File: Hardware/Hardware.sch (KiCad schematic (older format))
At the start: 68 parts

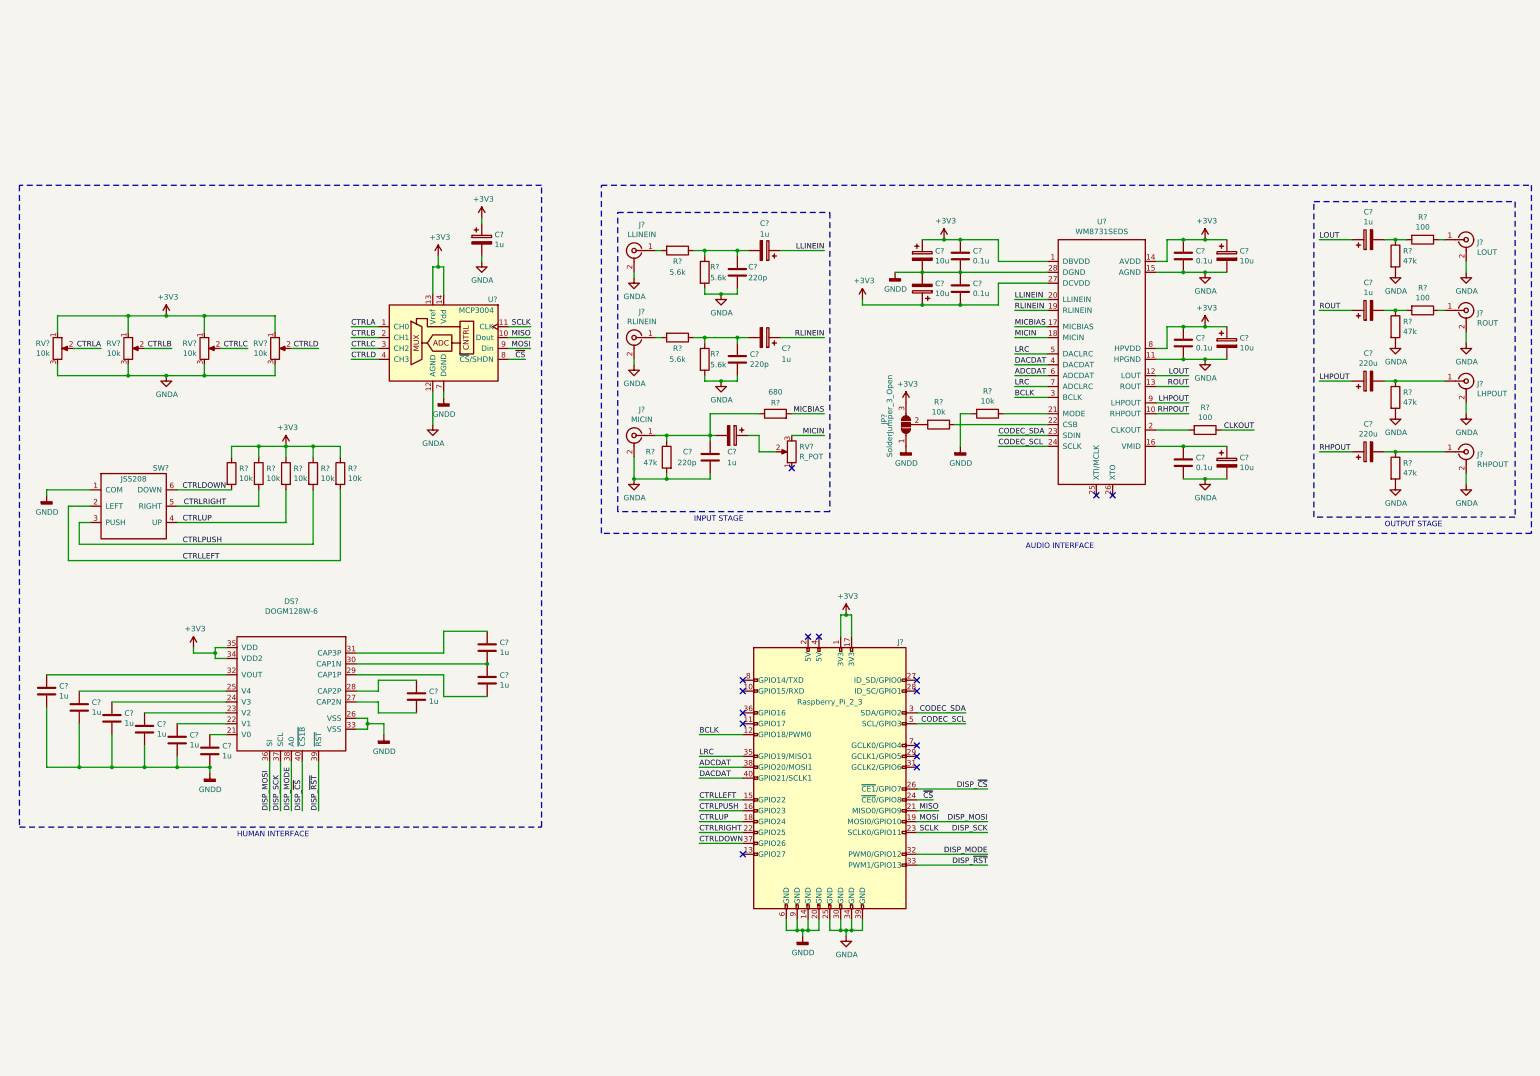
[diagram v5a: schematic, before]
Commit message: Assigned PCB footprints to schematic symbols
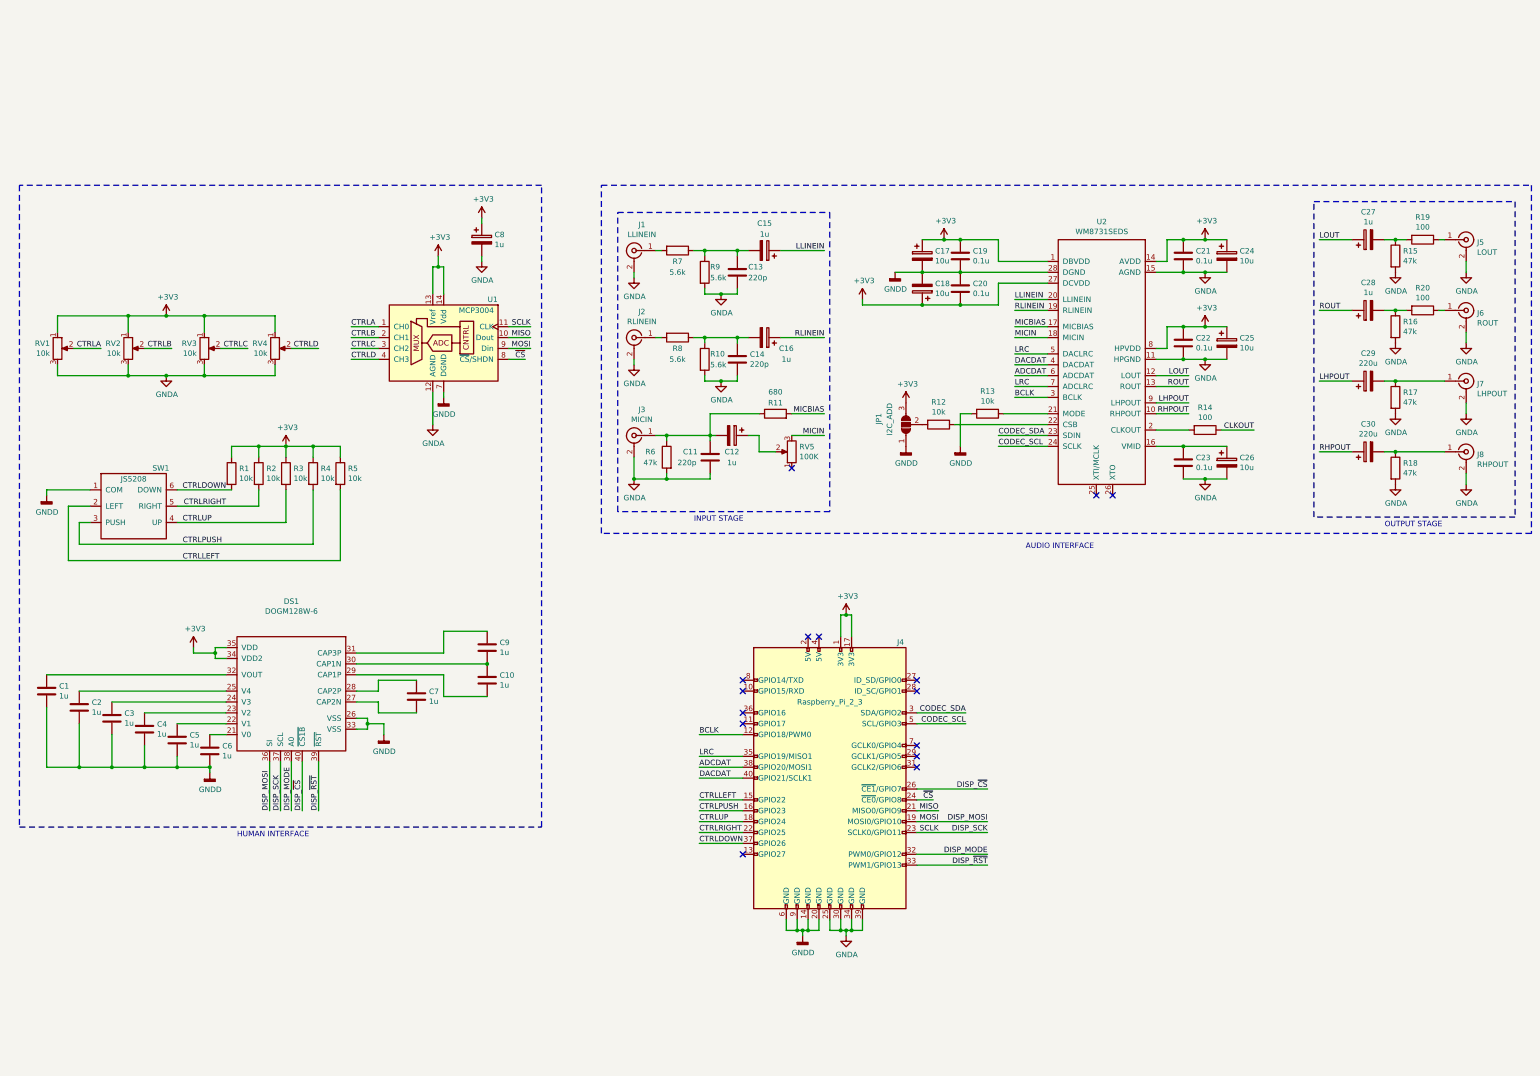
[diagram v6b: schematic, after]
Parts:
- C1, C10, C11, C13, C14, C2, C3, C4, C5, C6, C7, C9: renamed from C?; footprint (none) -> Capacitor_SMD:C_0603_1608Metric_Pad1.05x0.95mm_HandSolder
- C12, C15, C16, C27, C28, C8: renamed from C?; footprint (none) -> Capacitor_Tantalum_SMD:CP_EIA-3528-12_Kemet-T_Pad1.50x2.35mm_HandSolder
- C17, C18, C24, C25, C26: renamed from C?; footprint (none) -> Capacitor_Tantalum_SMD:CP_EIA-7343-15_Kemet-W_Pad2.25x2.55mm_HandSolder
- C19, C20, C21, C22, C23: renamed from C?; footprint (none) -> Capacitor_SMD:C_0805_2012Metric_Pad1.15x1.40mm_HandSolder
- C29, C30: renamed from C?; footprint (none) -> Capacitor_SMD:CP_Elec_8x10
- DS1: renamed from DS?; footprint (none) -> signl:DOGM128W
- J1, J2, J3, J5, J6, J7, J8: renamed from J?; footprint (none) -> Connector_Molex:Molex_KK-254_AE-6410-02A_1x02_P2.54mm_Vertical
- JP1: renamed from JP?; value SolderJumper_3_Open -> I2C_ADD; footprint (none) -> Jumper:SolderJumper-3_P1.3mm_Open_RoundedPad1.0x1.5mm_NumberLabels
- R1, R10, R11, R12, R13, R14, R15, R16, R17, R18, R19, R2, R20, R3, R4, R5, R6, R7, R8, R9: renamed from R?; footprint (none) -> Resistor_SMD:R_0805_2012Metric_Pad1.15x1.40mm_HandSolder
- RV1, RV2, RV3, RV4: renamed from RV?; footprint (none) -> Connector_Molex:Molex_KK-254_AE-6410-03A_1x03_P2.54mm_Vertical
- RV5: renamed from RV?; value R_POT -> 100K; footprint (none) -> Connector_Molex:Molex_KK-254_AE-6410-03A_1x03_P2.54mm_Vertical
- SW1: renamed from SW?; footprint (none) -> signl:JS5208
- gave numbers to parts that had none: 3

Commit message: Changed to using 3-pin connectors for LINEIN and HP. Footprint associations, Schematic PDF, Netlist updated.
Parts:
- removed J1: LLINEIN, Connector_Molex:Molex_KK-254_AE-6410-02A_1x02_P2.54mm_Vertical, symbol Connector:Conn_Coaxial
- removed J2: RLINEIN, Connector_Molex:Molex_KK-254_AE-6410-02A_1x02_P2.54mm_Vertical, symbol Connector:Conn_Coaxial
- removed J5: LOUT, Connector_Molex:Molex_KK-254_AE-6410-02A_1x02_P2.54mm_Vertical, symbol Connector:Conn_Coaxial
- removed J6: ROUT, Connector_Molex:Molex_KK-254_AE-6410-02A_1x02_P2.54mm_Vertical, symbol Connector:Conn_Coaxial
- removed J7: LHPOUT, Connector_Molex:Molex_KK-254_AE-6410-02A_1x02_P2.54mm_Vertical, symbol Connector:Conn_Coaxial
- removed J8: RHPOUT, Connector_Molex:Molex_KK-254_AE-6410-02A_1x02_P2.54mm_Vertical, symbol Connector:Conn_Coaxial
- added J1: LINEIN, Connector_Molex:Molex_KK-254_AE-6410-03A_1x03_P2.54mm_Vertical, symbol Connector:Conn_Coaxial_x2
- added J4: LOUT, Connector_Molex:Molex_KK-254_AE-6410-03A_1x03_P2.54mm_Vertical, symbol Connector:Conn_Coaxial_x2
- added J5: HPOUT, Connector_Molex:Molex_KK-254_AE-6410-03A_1x03_P2.54mm_Vertical, symbol Connector:Conn_Coaxial_x2
- renumbered J3 to J2, J4 to J3
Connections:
- net GNDA: now also J1.3 (EXT), J4.3 (EXT), J5.3 (EXT)
- net at R7.2: now also J1.1 (IN1)
- net at R8.2: now also J1.2 (IN2)
- net at R19.1: now also J4.1 (IN1)
- net at R20.1: now also J4.2 (IN2)
- net at C29.2, R17.1: now also J5.1 (IN1)
- net at C30.2, R18.1: now also J5.2 (IN2)
